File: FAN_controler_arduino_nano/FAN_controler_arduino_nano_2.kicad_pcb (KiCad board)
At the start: 2 copper layers, 97.6 x 62 mm, 17 parts, among them J1 Barrel_Jack_MountingPin, SW1 SW_Push

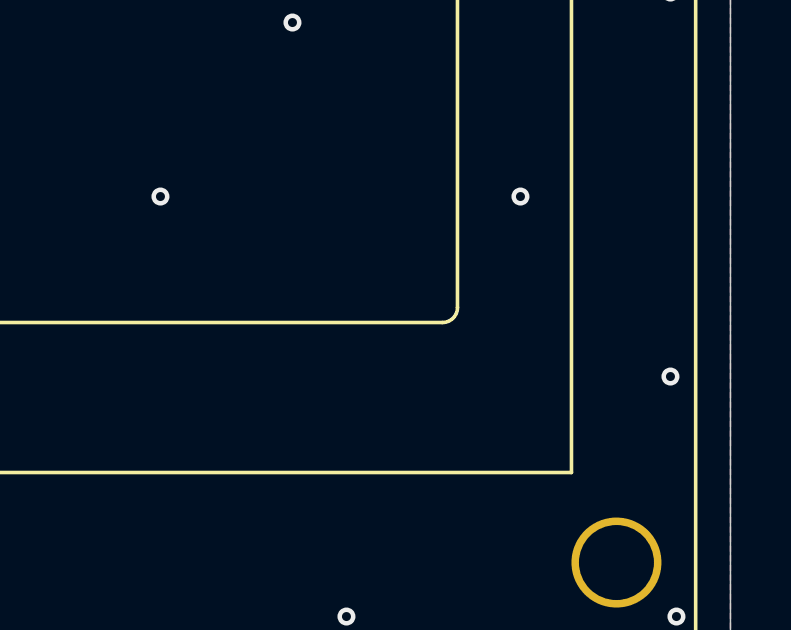
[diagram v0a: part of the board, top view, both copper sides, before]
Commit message: delete silk
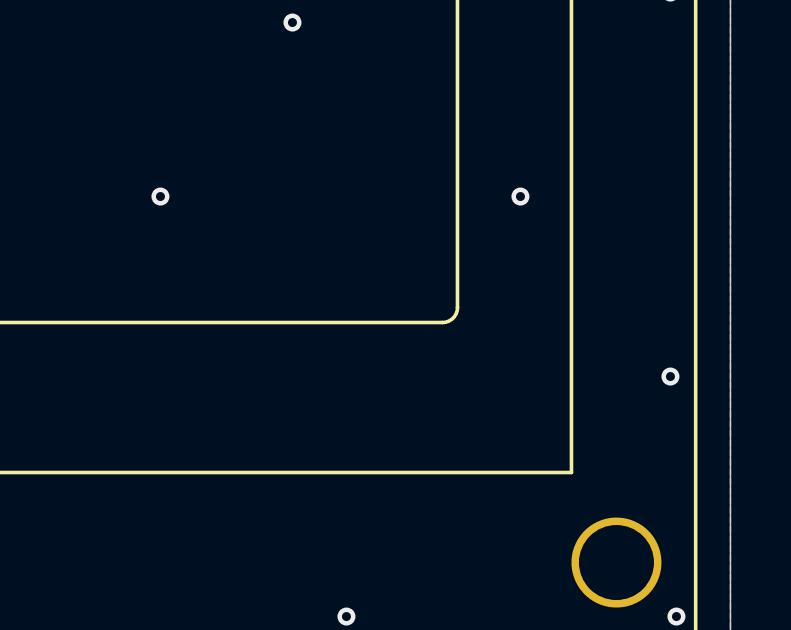
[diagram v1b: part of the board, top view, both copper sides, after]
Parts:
- moved G*** 2.45 mm to (132.7, 122.6)
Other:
- board text added: "R4p1"
